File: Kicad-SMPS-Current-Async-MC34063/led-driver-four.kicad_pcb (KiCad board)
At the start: 2 copper layers, 35 x 80 mm, 80 parts, among them J1 Input 12V-30V, J2 Output, J3 Conn_01x01, U1 MC34063, U2 LM321

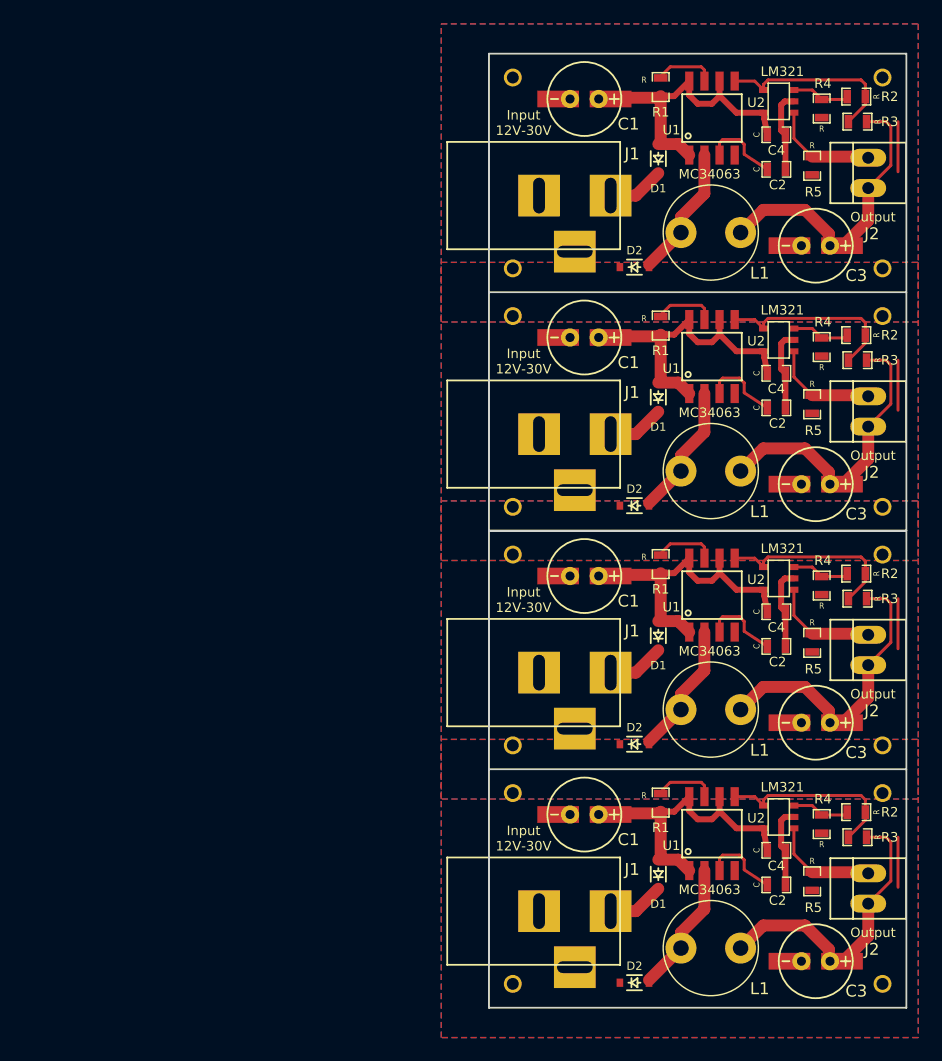
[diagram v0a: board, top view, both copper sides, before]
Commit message: Fix problem with current limiting resistor and also silk screen of diodes.
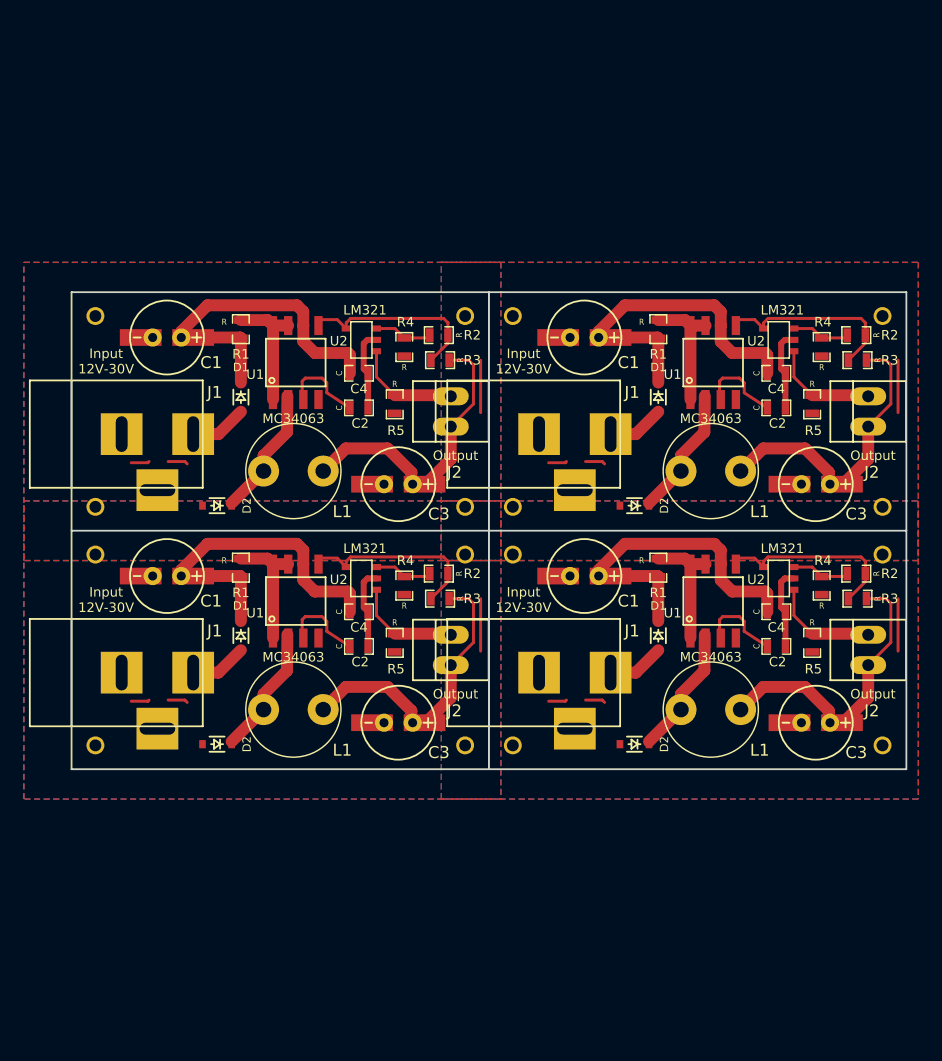
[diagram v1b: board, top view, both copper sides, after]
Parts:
- removed the C1 at (132.0, 71.3)
- removed the C1 at (132.0, 131.3)
- removed the C2 at (148.1, 77.2)
- removed the C2 at (148.1, 137.2)
- removed the C3 at (151.4, 83.6)
- removed the C3 at (151.4, 143.6)
- removed the C4 at (148.1, 74.3)
- removed the C4 at (148.1, 134.3)
- removed the D1 at (138.2, 76.3)
- removed the D1 at (138.2, 136.3)
- removed the D2 at (136.2, 85.4)
- removed the D2 at (136.2, 145.4)
- removed the J1 at (128.0, 79.4)
- removed the J1 at (128.0, 139.4)
- removed the J2 at (155.8, 77.5)
- removed the J2 at (155.8, 137.5)
- removed the J3 at (157.0, 145.5)
- removed the J3 at (126.0, 145.5)
- removed the J3 at (126.0, 129.5)
- removed the J3 at (157.0, 129.5)
- removed the J3 at (157.0, 85.5)
- removed the J3 at (126.0, 85.5)
- removed the J3 at (126.0, 69.5)
- removed the J3 at (157.0, 69.5)
- removed the L1 at (140.1, 82.5)
- removed the L1 at (140.1, 142.5)
- removed the R1 at (138.4, 90.3)
- removed the R1 at (138.4, 70.3)
- removed the R1 at (138.4, 130.3)
- removed the R2 at (154.8, 71.1)
- removed the R2 at (154.8, 131.1)
- removed the R3 at (154.9, 73.2)
- removed the R3 at (154.9, 133.2)
- removed the R4 at (151.9, 72.1)
- removed the R4 at (151.9, 132.1)
- removed the R5 at (151.1, 76.9)
- removed the R5 at (151.1, 136.9)
- removed the U1 at (142.7, 92.9)
- removed the U1 at (142.7, 72.9)
- removed the U1 at (142.7, 132.9)
- removed the U2 at (148.3, 71.5)
- removed the U2 at (148.3, 131.5)
- added C1: CP, smps-current-source:RADIAL_TABBED_2.5mm_6.3mm, F.Cu at (97.0, 111.3)
- added C1: CP, smps-current-source:RADIAL_TABBED_2.5mm_6.3mm, F.Cu at (97.0, 91.3)
- added C2: C, smps-current-source:SM0603_Capa, F.Cu at (113.1, 117.2)
- added C2: C, smps-current-source:SM0603_Capa, F.Cu at (113.1, 97.2)
- added C3: CP, smps-current-source:RADIAL_TABBED_2.5mm_6.3mm, F.Cu at (116.4, 123.6)
- added C3: CP, smps-current-source:RADIAL_TABBED_2.5mm_6.3mm, F.Cu at (116.4, 103.6)
- added C4: C, smps-current-source:SM0603_Capa, F.Cu at (113.1, 114.3)
- added C4: C, smps-current-source:SM0603_Capa, F.Cu at (113.1, 94.3)
- added D1: CUS15S30, smps-current-source:SOD-323, F.Cu at (103.2, 116.3)
- added D1: CUS15S30, smps-current-source:SOD-323, F.Cu at (103.2, 96.3)
- added D2: CUS15S30, smps-current-source:SOD-323, F.Cu at (101.2, 125.4)
- added D2: CUS15S30, smps-current-source:SOD-323, F.Cu at (101.2, 105.4)
- added J1: Input 12V-30V, smps-current-source:BARREL_JACK, F.Cu at (93.0, 119.4)
- added J1: Input 12V-30V, smps-current-source:BARREL_JACK, F.Cu at (93.0, 99.4)
- added J2: Output, smps-current-source:PINHEAD1-2, F.Cu at (120.8, 117.5)
- added J2: Output, smps-current-source:PINHEAD1-2, F.Cu at (120.8, 97.5)
- added J3: Conn_01x01, smps-current-source:THROUGHVIA, F.Cu at (122.0, 125.5)
- added J3: Conn_01x01, smps-current-source:THROUGHVIA, F.Cu at (91.0, 125.5)
- added J3: Conn_01x01, smps-current-source:THROUGHVIA, F.Cu at (91.0, 109.5)
- added J3: Conn_01x01, smps-current-source:THROUGHVIA, F.Cu at (122.0, 109.5)
- added J3: Conn_01x01, smps-current-source:THROUGHVIA, F.Cu at (122.0, 89.5)
- added J3: Conn_01x01, smps-current-source:THROUGHVIA, F.Cu at (91.0, 89.5)
- added J3: Conn_01x01, smps-current-source:THROUGHVIA, F.Cu at (91.0, 105.5)
- added J3: Conn_01x01, smps-current-source:THROUGHVIA, F.Cu at (122.0, 105.5)
- added L1: L, smps-current-source:L_Radial_D7.8mm_P5.00mm_Fastron_07HCP, F.Cu at (105.1, 122.5)
- added L1: L, smps-current-source:L_Radial_D7.8mm_P5.00mm_Fastron_07HCP, F.Cu at (105.1, 102.5)
- added R1: R, smps-current-source:SM0603_Resistor, F.Cu at (103.2, 110.6)
- added R1: R, smps-current-source:SM0603_Resistor, F.Cu at (103.2, 90.6)
- added R1: R, smps-current-source:SM0603_Resistor, F.Cu at (138.2, 90.6)
- added R2: R, smps-current-source:SM0603_Resistor, F.Cu at (119.8, 111.1)
- added R2: R, smps-current-source:SM0603_Resistor, F.Cu at (119.8, 91.1)
- added R3: R, smps-current-source:SM0603_Resistor, F.Cu at (119.9, 113.2)
- added R3: R, smps-current-source:SM0603_Resistor, F.Cu at (119.9, 93.2)
- added R4: R, smps-current-source:SM0603_Resistor, F.Cu at (116.9, 112.1)
- added R4: R, smps-current-source:SM0603_Resistor, F.Cu at (116.9, 92.1)
- added R5: R, smps-current-source:SM0603_Resistor, F.Cu at (116.1, 116.9)
- added R5: R, smps-current-source:SM0603_Resistor, F.Cu at (116.1, 96.9)
- added U1: MC34063, smps-current-source:SOIC_08_4.0mm_5.0mm_1.27mm, F.Cu at (107.8, 113.4)
- added U1: MC34063, smps-current-source:SOIC_08_4.0mm_5.0mm_1.27mm, F.Cu at (107.8, 93.4)
- added U1: MC34063, smps-current-source:SOIC_08_4.0mm_5.0mm_1.27mm, F.Cu at (142.8, 93.4)
- added U2: LM321, smps-current-source:SOT23-5, F.Cu at (113.3, 111.5)
- added U2: LM321, smps-current-source:SOT23-5, F.Cu at (113.3, 91.5)
- moved U1 0.51 mm to (142.8, 113.4)
- moved R1 0.36 mm to (138.2, 110.6)
- turned D1 to 90 degrees (x2)
- turned D2 to 0 degrees (x2)
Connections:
- U1 pad 1: /Vcc -> Net-(R1-Pad1)
- U1 pad 8: /Vcc -> Net-(R1-Pad1)
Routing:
- net Net-(R1-Pad1): track 20.7 -> 41.4 mm
- net (no net): track 16.8 -> 30.5 mm
- net /Vcc: track 108.2 -> 116.1 mm
- net Net-(D2-Pad1): track 45.3 -> 44.5 mm
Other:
- board size 35 x 80 mm -> 70 x 40 mm
